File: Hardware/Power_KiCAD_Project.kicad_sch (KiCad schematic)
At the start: 7 parts, among them J1 Barrel_Jack_MountingPin, J2 XT60 Cell 5, J3 XT60 Cell 4, J4 XT60 Cell 3, J5 XT60 Cell 2, J6 XT60 Cell 1, J7 XT60 To External Switch

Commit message: Test
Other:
- note added: "Github Commit Practice"
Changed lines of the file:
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@@
     (stroke (width 0) (type default) (color 0 0 0 0))
+  )
+  (text "Github Commit Practice" (at 189.23 124.46 0)
+    (effects (font (size 1.27 1.27)) (justify left bottom))
   )
   (text "Battery Pack Connectors" (at 118.11 129.54 0)

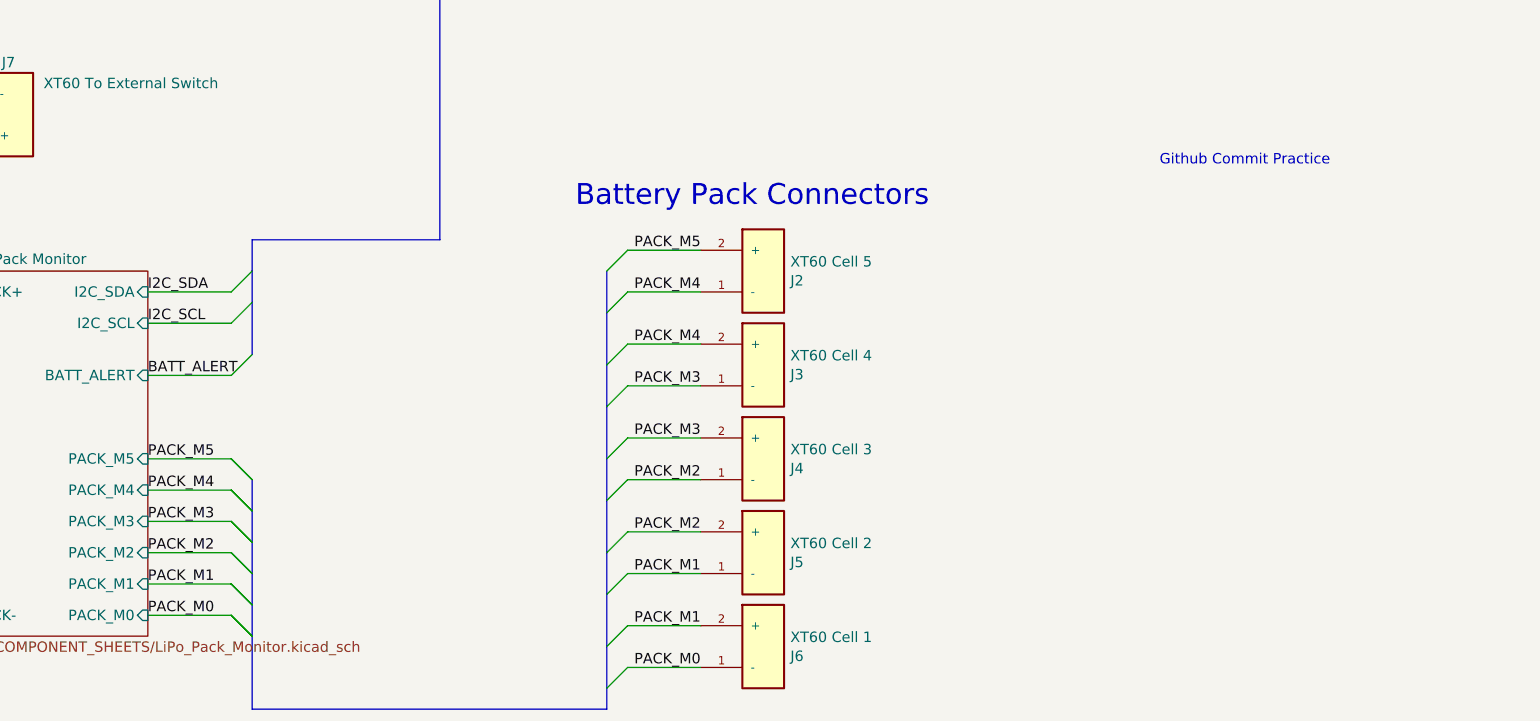
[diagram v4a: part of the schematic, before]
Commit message: Removed LiPo connectors 4 and 5, flipped connectors
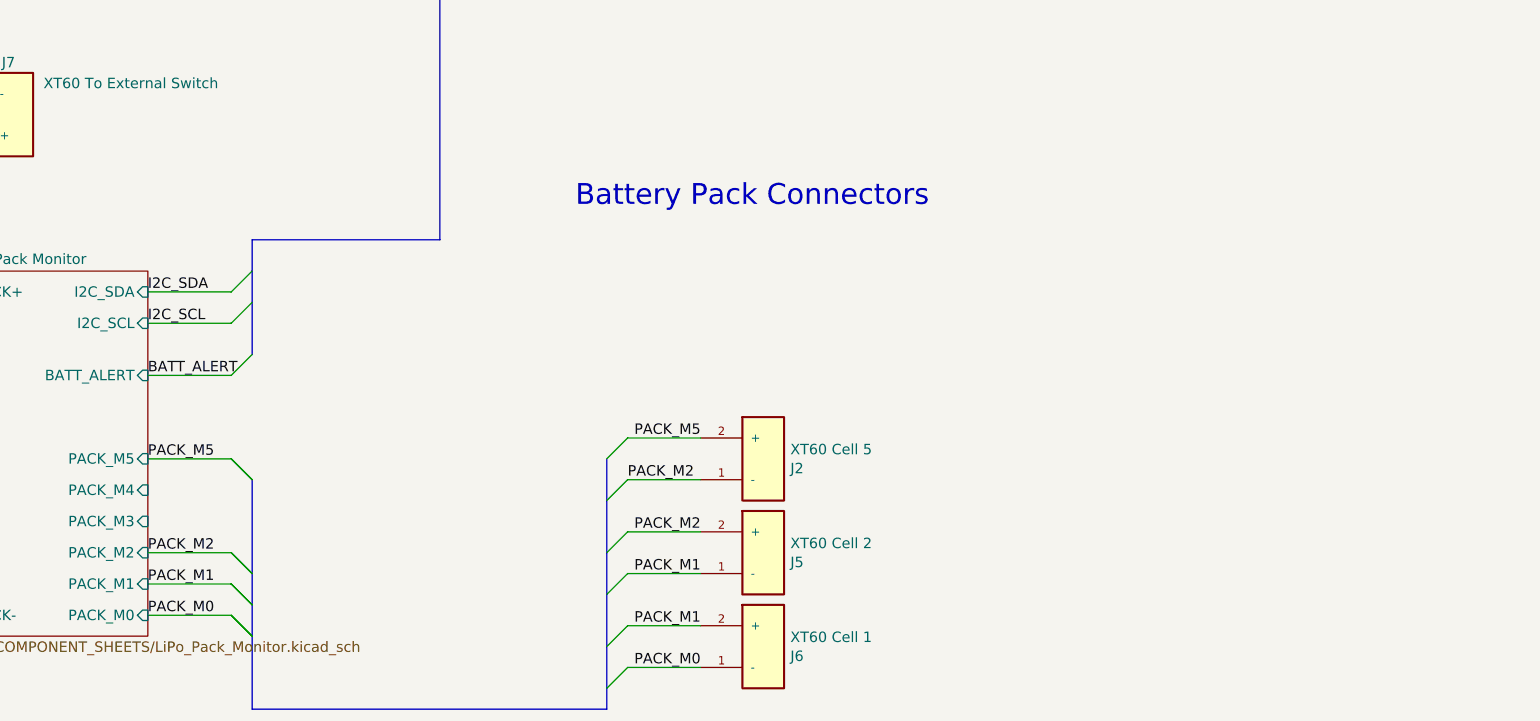
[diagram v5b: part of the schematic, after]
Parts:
- removed J3: XT60 Cell 4, RDT_Custom_Footprints:AMASS_XT60-M, symbol Power_KiCAD_Project-rescue:XT60-M-XT60-M-Power_KiCAD_Project-rescue
- removed J4: XT60 Cell 3, RDT_Custom_Footprints:AMASS_XT60-M, symbol Power_KiCAD_Project-rescue:XT60-M-XT60-M-Power_KiCAD_Project-rescue
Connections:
- net PACK_M4 is gone; now on net PACK_M2: J2.1 (-)
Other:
- note removed: "Github Commit Practice"
- moved on the sheet: J2
